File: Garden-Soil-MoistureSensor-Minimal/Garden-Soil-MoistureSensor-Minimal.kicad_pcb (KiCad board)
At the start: 2 copper layers, 6 parts, among them J1 Conn_01x15, J2 Conn_01x15, J3 Screw_Terminal_01x02, U1 1043

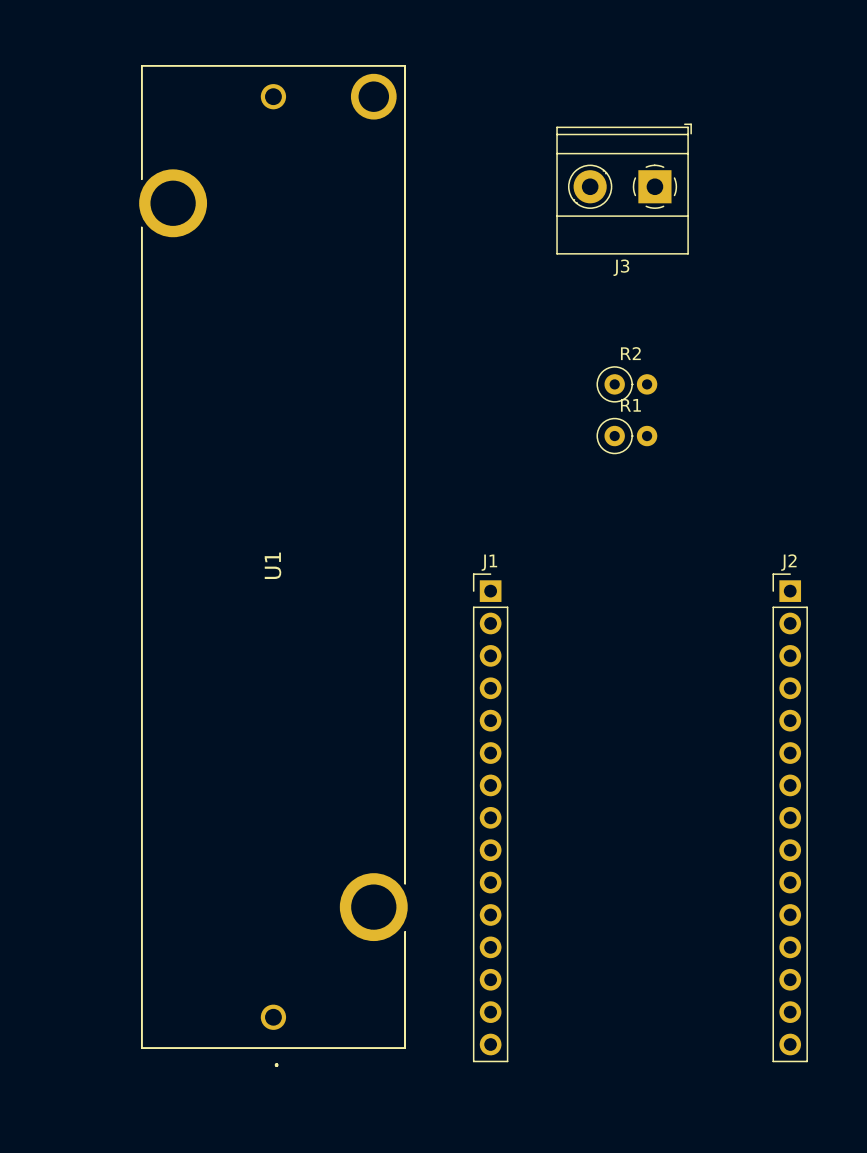
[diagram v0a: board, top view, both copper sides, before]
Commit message: simple meter made DRCed and fab files put in. This seems like a waste to have fabbed for a single area but since i made the schematic people can make this on a bread board faster and cheaper then having this fabbed.
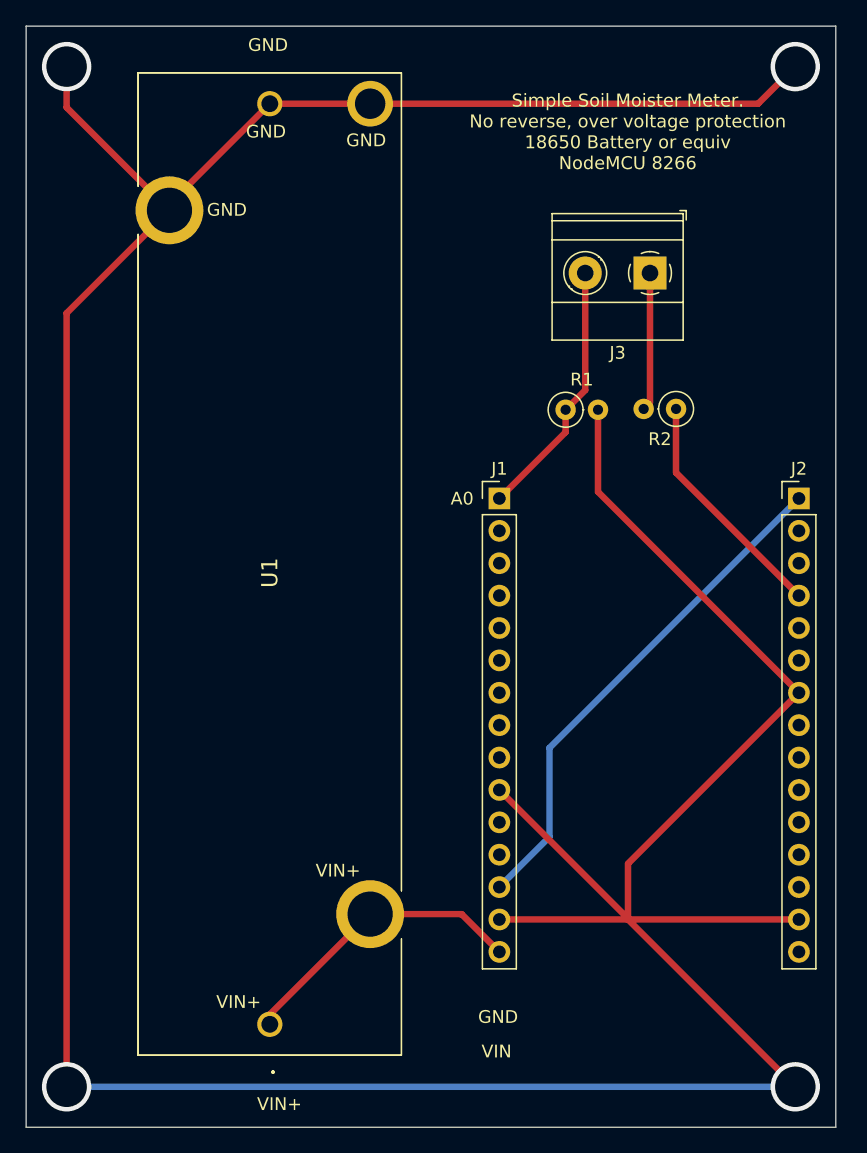
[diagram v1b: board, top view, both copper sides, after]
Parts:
- moved J1 7.30 mm to (151.4, 87.8)
- moved J2 7.30 mm to (174.9, 87.8)
- moved J3 6.78 mm to (163.2, 70.2)
- moved R2 5.18 mm to (165.3, 80.8), turned to 180 degrees
- moved R1 4.37 mm to (156.6, 80.9)
- moved U1 0.62 mm to (133.4, 129.1)
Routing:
- net GND: track 0.00 -> 306.3 mm, vias 0 -> 4
- net DO: track 0.00 -> 40.2 mm
- net VIN: track 0.00 -> 23.3 mm
- net A0: track 0.00 -> 20.5 mm
- net D3: track 0.00 -> 18.6 mm
- net Net-(R2-Pad2): track 0.00 -> 10.9 mm
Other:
- board outline added: 63.5 x 86.4 mm
- board text added: "A0"
- board text added: "GND"
- board text added: "Simple Soil Moister Meter. No reverse, over voltage protection 18650 Battery or equiv NodeMCU 8266"
- board text added: "VIN"
- board text added: "VIN+"
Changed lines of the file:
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@@
   )
   (setup
+    (stackup
+      (layer "F.SilkS" (type "Top Silk Screen"))
+      (layer "F.Paste" (type "Top Solder Paste"))
+      (layer "F.Mask" (type "Top Solder Mask") (thickness 0.01))
+      (layer "F.Cu" (type "copper") (thickness 0.035))
+      (layer "dielectric 1" (type "core") (thickness 1.51) (material "FR4") (epsilon_r 4.5) (loss_tangent 0.02))
+      (layer "B.Cu" (type "copper") (thickness 0.035))
+      (layer "B.Mask" (type "Bottom Solder Mask") (thickness 0.01))
+      (layer "B.Paste" (type "Bottom Solder Paste"))
+      (layer "B.SilkS" (type "Bottom Silk Screen"))
+      (copper_finish "None")
+      (dielectric_constraints no)
+    )
     (pad_to_mask_clearance 0)
     (pcbplotparams
@@
   (net 27 "Net-(R2-Pad2)")
   (footprint "Connector_PinHeader_2.54mm:PinHeader_1x15_P2.54mm_Vertical" (layer "F.Cu")
-    (at 174.224989 95.110432)
+    (at 174.909169 87.843538)
     (descr "Through hole straight pin header, 1x15, 2.54mm pitch, single row")
     (tags "Through hole pin header THT 1x15 2.54mm single row")
@@
   )
   (footprint "Resistor_THT:R_Axial_DIN0207_L6.3mm_D2.5mm_P2.54mm_Vertical" (layer "F.Cu")
-    (at 160.459643 78.897644)
+    (at 165.273403 80.822193 180)
     (descr "Resistor, Axial_DIN0207 series, Axial, Vertical, pin pitch=2.54mm, 0.25W = 1/4W, length*diameter=6.3*2.5mm^2, http://cdn-reichelt.de/documents/datenblatt/B400/1_4W%23YAG.pdf")
     (tags "Resistor Axial_DIN0207 series Axial Vertical pin pitch 2.54mm 0.25W = 1/4W length 6.3mm diameter 2.5mm")
@@
     (fp_line (start 0 0) (end 2.54 0) (layer "F.Fab") (width 0.1))
     (fp_circle (center 0 0) (end 1.25 0) (layer "F.Fab") (width 0.1) (fill none))
-    (pad "1" thru_hole circle locked (at 0 0) (size 1.6 1.6) (drill 0.8) (layers *.Cu *.Mask)
+    (pad "1" thru_hole circle locked (at 0 0 180) (size 1.6 1.6) (drill 0.8) (layers *.Cu *.Mask)
       (net 17 "D3") (pintype "passive"))
-    (pad "2" thru_hole oval locked (at 2.54 0) (size 1.6 1.6) (drill 0.8) (layers *.Cu *.Mask)
+    (pad "2" thru_hole oval locked (at 2.54 0 180) (size 1.6 1.6) (drill 0.8) (layers *.Cu *.Mask)
       (net 27 "Net-(R2-Pad2)") (pintype "passive"))
     (model "${KICAD6_3DMODEL_DIR}/Resistor_THT.3dshapes/R_Axial_DIN0207_L6.3mm_D2.5mm_P2.54mm_Vertical.wrl"
@@
   )
   (footprint "Resistor_THT:R_Axial_DIN0207_L6.3mm_D2.5mm_P2.54mm_Vertical" (layer "F.Cu")
-    (at 160.459643 82.947644)
+    (at 156.610887 80.886404)
     (descr "Resistor, Axial_DIN0207 series, Axial, Vertical, pin pitch=2.54mm, 0.25W = 1/4W, length*diameter=6.3*2.5mm^2, http://cdn-reichelt.de/documents/datenblatt/B400/1_4W%23YAG.pdf")
     (tags "Resistor Axial_DIN0207 series Axial Vertical pin pitch 2.54mm 0.25W = 1/4W length 6.3mm diameter 2.5mm")
@@
   )
   (footprint "TerminalBlock_Phoenix:TerminalBlock_Phoenix_MKDS-1,5-2-5.08_1x02_P5.08mm_Horizontal" (layer "F.Cu")
-    (at 163.615923 63.397864 180)
+    (at 163.229139 70.164314 180)
     (descr "Terminal Block Phoenix MKDS-1,5-2-5.08, 2 pins, pitch 5.08mm, size 10.2x9.8mm^2, drill diamater 1.3mm, pad diameter 2.6mm, see http://www.farnell.com/datasheets/100425.pdf, script-generated using https://github.com/pointhi/kicad-footprint-generator/scripts/TerminalBlock_Phoenix")
     (tags "THT Terminal Block Phoenix MKDS-1,5-2-5.08 pitch 5.08mm size 10.2x9.8mm^2 drill 1.3mm pad 2.6mm")
@@
   )
   (footprint "Connector_PinHeader_2.54mm:PinHeader_1x15_P2.54mm_Vertical" (layer "F.Cu")
-    (at 150.729989 95.110432)
+    (at 151.414169 87.843538)
     (descr "Through hole straight pin header, 1x15, 2.54mm pitch, single row")
     (tags "Through hole pin header THT 1x15 2.54mm single row")
@@
   )
   (footprint "SamacSys_Parts:1043" (layer "F.Cu")
-    (at 133.696164 128.533301 90)
+    (at 133.410944 129.084219 90)
     (descr "1043-3")
     (tags "Undefined or Miscellaneous")
@@
     )
   )
+  (gr_line (start 177.8 137.16) (end 177.8 50.8) (layer "Edge.Cuts") (width 0.1))
+  (gr_line (start 114.3 50.8) (end 114.3 137.16) (layer "Edge.Cuts") (width 0.1))
+  (gr_line (start 114.3 50.8) (end 177.8 50.8) (layer "Edge.Cuts") (width 0.1))
+  (gr_line (start 114.3 137.16) (end 177.8 137.16) (layer "Edge.Cuts") (width 0.1))
+  (gr_text "GND" (at 133.272651 52.279804) (layer "F.SilkS")
+    (effects (font (size 1 1) (thickness 0.15)))
+  )
+  (gr_text "VIN" (at 151.195027 131.216615) (layer "F.SilkS")
+    (effects (font (size 1 1) (thickness 0.15)))
+  )
+  (gr_text "VIN+" (at 130.966741 127.336668) (layer "F.SilkS")
+    (effects (font (size 1 1) (thickness 0.15)))
+  )
+  (gr_text "Simple Soil Moister Meter. \nNo reverse, over voltage protection \n18650 Battery or equiv\nNodeMCU 8266" (at 161.483382 59.089595) (layer "F.SilkS")
+    (effects (font (size 1.016 1.016) (thickness 0.254)))
+  )
+  (gr_text "GND" (at 130.045809 65.207218) (layer "F.SilkS")
+    (effects (font (size 1 1) (thickness 0.15)))
+  )
+  (gr_text "GND" (at 133.112311 59.074212) (layer "F.SilkS")
+    (effects (font (size 1 1) (thickness 0.15)))
+  )
+  (gr_text "VIN+" (at 134.165247 135.344229) (layer "F.SilkS")
+    (effects (font (size 1 1) (thickness 0.15)))
+  )
+  (gr_text "GND" (at 151.315282 128.510877) (layer "F.SilkS")
+    (effects (font (size 1 1) (thickness 0.15)))
+  )
+  (gr_text "VIN+" (at 138.76335 117.034898) (layer "F.SilkS")
+    (effects (font (size 1 1) (thickness 0.15)))
+  )
+  (gr_text "A0" (at 148.495237 87.856853) (layer "F.SilkS")
+    (effects (font (size 1 1) (thickness 0.15)))
+  )
+  (gr_text "GND" (at 140.968972 59.755657) (layer "F.SilkS")
+    (effects (font (size 1 1) (thickness 0.15)))
+  )
+  (segment (start 156.610887 80.886404) (end 156.610887 82.64682) (width 0.508) (layer "F.Cu") (net 1))
+  (segment (start 158.149139 79.348152) (end 156.610887 80.886404) (width 0.508) (layer "F.Cu") (net 1))
+  (segment (start 158.149139 70.164314) (end 158.149139 79.348152) (width 0.508) (layer "F.Cu") (net 1))
+  (segment (start 156.610887 82.64682) (end 151.414169 87.843538) (width 0.508) (layer "F.Cu") (net 1))
+  (segment (start 151.414169 120.863538) (end 161.503538 120.863538) (width 0.508) (layer "F.Cu") (net 10))
+  (segment (start 174.909169 103.083538) (end 161.503538 116.489169) (width 0.508) (layer "F.Cu") (net 10))
+  (segment (start 161.503538 120.863538) (end 161.503538 120.792907) (width 0.508) (layer "F.Cu") (net 10))
+  (segment (start 117.475 73.310163) (end 117.475 133.985) (width 0.508) (layer "F.Cu") (net 10))
+  (segment (start 125.540944 64.754219) (end 125.540944 65.244219) (width 0.508) (layer "F.Cu") (net 10))
+  (segment (start 117.475 57.178275) (end 125.540944 65.244219) (width 0.508) (layer "F.Cu") (net 10))
+  (segment (start 174.909169 120.863538) (end 161.503538 120.863538) (width 0.508) (layer "F.Cu") (net 10))
+  (segment (start 171.715781 56.884219) (end 141.280944 56.884219) (width 0.508) (layer "F.Cu") (net 10))
+  (segment (start 161.503538 120.792907) (end 151.414169 110.703538) (width 0.508) (layer "F.Cu") (net 10))
+  (segment (start 125.540944 65.244219) (end 117.475 73.310163) (width 0.508) (layer "F.Cu") (net 10))
+  (segment (start 159.150887 80.886404) (end 159.150887 87.325256) (width 0.508) (layer "F.Cu") (net 10))
+  (segment (start 117.475 53.975) (end 117.475 57.178275) (width 0.508) (layer "F.Cu") (net 10))
+  (segment (start 141.280944 56.884219) (end 133.410944 56.884219) (width 0.508) (layer "F.Cu") (net 10))
+  (segment (start 174.625 53.975) (end 171.715781 56.884219) (width 0.508) (layer "F.Cu") (net 10))
+  (segment (start 161.503538 120.863538) (end 174.625 133.985) (width 0.508) (layer "F.Cu") (net 10))
+  (segment (start 133.410944 56.884219) (end 125.540944 64.754219) (width 0.508) (layer "F.Cu") (net 10))
+  (segment (start 161.503538 116.489169) (end 161.503538 120.792907) (width 0.508) (layer "F.Cu") (net 10))
+  (segment (start 159.150887 87.325256) (end 174.909169 103.083538) (width 0.508) (layer "F.Cu") (net 10))
+  (via (at 117.475 53.975) (size 3.8736) (drill 3.175) (layers "F.Cu" "B.Cu") (free) (net 10))
+  (via (at 174.625 53.975) (size 3.8736) (drill 3.175) (layers "F.Cu" "B.Cu") (free) (net 10))
+  (via (at 174.625 133.985) (size 3.8736) (drill 3.175) (layers "F.Cu" "B.Cu") (free) (net 10))
+  (via (at 117.475 133.985) (size 3.8736) (drill 3.175) (layers "F.Cu" "B.Cu") (free) (net 10))
+  (segment (start 117.475 133.985) (end 174.625 133.985) (width 0.508) (layer "B.Cu") (net 10))
+  (segment (start 155.345537 114.39217) (end 151.414169 118.323538) (width 0.508) (layer "B.Cu") (net 13))
+  (segment (start 174.909169 87.843538) (end 155.345537 107.40717) (width 0.508) (layer "B.Cu") (net 13))
+  (segment (start 155.345537 107.40717) (end 155.345537 114.39217) (width 0.508) (layer "B.Cu") (net 13))
+  (segment (start 141.280944 120.444219) (end 148.45485 120.444219) (width 0.508) (layer "F.Cu") (net 14))
+  (segment (start 133.410944 128.314219) (end 133.410944 129.084219) (width 0.508) (layer "F.Cu") (net 14))
+  (segment (start 141.280944 120.444219) (end 133.410944 128.314219) (width 0.508) (layer "F.Cu") (net 14))
+  (segment (start 148.45485 120.444219) (end 151.414169 123.403538) (width 0.508) (layer "F.Cu") (net 14))
+  (segment (start 165.273403 85.827772) (end 174.909169 95.463538) (width 0.508) (layer "F.Cu") (net 17))
+  (segment (start 165.273403 80.822193) (end 165.273403 85.827772) (width 0.508) (layer "F.Cu") (net 17))
+  (segment (start 163.229139 80.326457) (end 162.733403 80.822193) (width 0.508) (layer "F.Cu") (net 27))
+  (segment (start 163.229139 70.164314) (end 163.229139 80.326457) (width 0.508) (layer "F.Cu") (net 27))
   (group "" (id 31916c38-883f-4186-ab10-8bd6d91959f5)
     (members
